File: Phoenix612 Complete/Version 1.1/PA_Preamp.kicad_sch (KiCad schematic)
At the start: 21 parts, among them J14 TP, J15 TP, U8 LT1253, U9 QPR_Filter

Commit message: Update 9Mar23
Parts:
- removed J14, J15: TP, Connector_PinHeader_1.00mm:PinHeader_1x01_P1.00mm_Vertical, symbol Connector_Generic:Conn_01x01
- added J14: TP11, Connector_PinSocket_2.54mm:PinSocket_1x02_P2.54mm_Vertical, symbol Connector_Generic:Conn_01x02
- added J15: TP12, Connector_PinSocket_2.54mm:PinSocket_1x02_P2.54mm_Vertical, symbol Connector_Generic:Conn_01x02
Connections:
- net GND: now also J14.2 (Pin_2), J15.2 (Pin_2)
- net PA_DRIVER_IN: now also J15.1 (Pin_1)
- net at C61.1, U9.7 (OUT), U9.8 (OUT): now also J14.1 (Pin_1)
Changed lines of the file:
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@@
   (junction (at 103.505 92.71) (diameter 0) (color 0 0 0 0)
   )
+  (junction (at 189.865 96.52) (diameter 0) (color 0 0 0 0)
+  )
   (junction (at 154.94 110.49) (diameter 0) (color 0 0 0 0)
   )
@@
   )
   (junction (at 139.065 92.71) (diameter 0) (color 0 0 0 0)
-  )
-  (junction (at 196.215 96.52) (diameter 0) (color 0 0 0 0)
   )
   (no_connect (at 180.34 111.125))
@@
     (stroke (width 0) (type default) (color 0 0 0 0))
   )
+  (wire (pts (xy 189.865 96.52) (xy 203.2 96.52))
+    (stroke (width 0) (type default) (color 0 0 0 0))
+  )
   (wire (pts (xy 161.29 83.82) (xy 152.4 83.82))
     (stroke (width 0) (type default) (color 0 0 0 0))
   )
+  (wire (pts (xy 139.065 90.805) (xy 139.065 92.71))
+    (stroke (width 0) (type default) (color 0 0 0 0))
+  )
   (wire (pts (xy 217.17 63.5) (xy 217.17 74.93))
     (stroke (width 0) (type default) (color 0 0 0 0))
@@
     (stroke (width 0) (type default) (color 0 0 0 0))
   )
+  (wire (pts (xy 130.81 90.805) (xy 139.065 90.805))
+    (stroke (width 0) (type default) (color 0 0 0 0))
+  )
   (wire (pts (xy 169.545 60.96) (xy 169.545 63.5))
     (stroke (width 0) (type default) (color 0 0 0 0))
@@
     (stroke (width 0) (type default) (color 0 0 0 0))
   )
+  (wire (pts (xy 189.865 83.185) (xy 189.865 96.52))
+    (stroke (width 0) (type default) (color 0 0 0 0))
+  )
   (wire (pts (xy 111.125 97.79) (xy 111.125 100.33))
     (stroke (width 0) (type default) (color 0 0 0 0))
@@
     (stroke (width 0) (type default) (color 0 0 0 0))
   )
+  (wire (pts (xy 130.81 80.645) (xy 130.81 90.805))
+    (stroke (width 0) (type default) (color 0 0 0 0))
+  )
   (wire (pts (xy 139.065 92.71) (xy 142.24 92.71))
     (stroke (width 0) (type default) (color 0 0 0 0))
@@
     (stroke (width 0) (type default) (color 0 0 0 0))
   )
-  (wire (pts (xy 196.215 96.52) (xy 203.2 96.52))
-    (stroke (width 0) (type default) (color 0 0 0 0))
-  )
   (wire (pts (xy 229.87 45.72) (xy 229.87 55.88))
     (stroke (width 0) (type default) (color 0 0 0 0))
@@
     (stroke (width 0) (type default) (color 0 0 0 0))
   )
-  (wire (pts (xy 186.69 96.52) (xy 196.215 96.52))
+  (wire (pts (xy 186.69 96.52) (xy 189.865 96.52))
     (stroke (width 0) (type default) (color 0 0 0 0))
   )
@@
   )
   (wire (pts (xy 131.445 105.41) (xy 131.445 100.33))
+    (stroke (width 0) (type default) (color 0 0 0 0))
+  )
+  (wire (pts (xy 133.35 80.645) (xy 133.35 83.185))
     (stroke (width 0) (type default) (color 0 0 0 0))
   )
@@
     (pin "1")
   )
+  (symbol (lib_id "power:GND") (at 192.405 83.185 0) (unit 1)
+    (in_bom yes) (on_board yes)
+    (property "Reference" "#PWR0107" (id 0) (at 192.405 89.535 0)
+      (effects (font (size 1.27 1.27)) hide)
+    )
+    (property "Value" "GND" (id 1) (at 192.405 86.995 0))
+    (property "Footprint" "" (id 2) (at 192.405 83.185 0)
+      (effects (font (size 1.27 1.27)) hide)
+    )
+    (property "Datasheet" "" (id 3) (at 192.405 83.185 0)
+      (effects (font (size 1.27 1.27)) hide)
+    )
+    (pin "1")
+  )
   (symbol (lib_id "Custom_RF:LT1253") (at 207.645 59.69 0) (unit 3)
     (in_bom yes) (on_board yes) (fields_autoplaced)
@@
     (pin "2")
   )
-  (symbol (lib_id "Connector_Generic:Conn_01x01") (at 139.065 87.63 90) (unit 1)
-    (in_bom yes) (on_board yes) (fields_autoplaced)
-    (property "Reference" "J14" (id 0) (at 141.605 86.3599 90)
-      (effects (font (size 1.27 1.27)) (justify right))
-    )
-    (property "Value" "TP" (id 1) (at 141.605 88.8999 90)
-      (effects (font (size 1.27 1.27)) (justify right))
-    )
-    (property "Footprint" "Connector_PinHeader_1.00mm:PinHeader_1x01_P1.00mm_Vertical" (id 2) (at 139.065 87.63 0)
-      (effects (font (size 1.27 1.27)) hide)
-    )
-    (property "Datasheet" "~" (id 3) (at 139.065 87.63 0)
-      (effects (font (size 1.27 1.27)) hide)
-    )
-    (pin "1")
-  )
   (symbol (lib_id "Device:C") (at 169.545 67.31 0) (unit 1)
     (in_bom yes) (on_board yes) (fields_autoplaced)
@@
     )
     (property "Datasheet" "" (id 3) (at 152.4 73.66 0)
-      (effects (font (size 1.27 1.27)) hide)
-    )
-    (pin "1")
-  )
-  (symbol (lib_id "Connector_Generic:Conn_01x01") (at 196.215 91.44 90) (unit 1)
-    (in_bom yes) (on_board yes) (fields_autoplaced)
-    (property "Reference" "J15" (id 0) (at 198.755 90.1699 90)
-      (effects (font (size 1.27 1.27)) (justify right))
-    )
-    (property "Value" "TP" (id 1) (at 198.755 92.7099 90)
-      (effects (font (size 1.27 1.27)) (justify right))
-    )
-    (property "Footprint" "Connector_PinHeader_1.00mm:PinHeader_1x01_P1.00mm_Vertical" (id 2) (at 196.215 91.44 0)
-      (effects (font (size 1.27 1.27)) hide)
-    )
-    (property "Datasheet" "~" (id 3) (at 196.215 91.44 0)
       (effects (font (size 1.27 1.27)) hide)
     )
@@
     )
     (property "Datasheet" "~" (id 3) (at 161.29 71.12 0)
+      (effects (font (size 1.27 1.27)) hide)
+    )
+    (pin "1")
+    (pin "2")
+  )
+  (symbol (lib_id "Connector_Generic:Conn_01x02") (at 189.865 78.105 90) (unit 1)
+    (in_bom yes) (on_board yes) (fields_autoplaced)
+    (property "Reference" "J15" (id 0) (at 195.58 76.8349 90)
+      (effects (font (size 1.27 1.27)) (justify right))
+    )
+    (property "Value" "TP12" (id 1) (at 195.58 79.3749 90)
+      (effects (font (size 1.27 1.27)) (justify right))
+    )
+    (property "Footprint" "Connector_PinSocket_2.54mm:PinSocket_1x02_P2.54mm_Vertical" (id 2) (at 189.865 78.105 0)
+      (effects (font (size 1.27 1.27)) hide)
+    )
+    (property "Datasheet" "~" (id 3) (at 189.865 78.105 0)
       (effects (font (size 1.27 1.27)) hide)
     )
@@
     (pin "1")
   )
+  (symbol (lib_id "power:GND") (at 133.35 83.185 0) (unit 1)
+    (in_bom yes) (on_board yes)
+    (property "Reference" "#PWR0106" (id 0) (at 133.35 89.535 0)
+      (effects (font (size 1.27 1.27)) hide)
+    )
+    (property "Value" "GND" (id 1) (at 133.35 86.995 0))
+    (property "Footprint" "" (id 2) (at 133.35 83.185 0)
+      (effects (font (size 1.27 1.27)) hide)
+    )
+    (property "Datasheet" "" (id 3) (at 133.35 83.185 0)
+      (effects (font (size 1.27 1.27)) hide)
+    )
+    (pin "1")
+  )
+  (symbol (lib_id "Connector_Generic:Conn_01x02") (at 130.81 75.565 90) (unit 1)
+    (in_bom yes) (on_board yes)
+    (property "Reference" "J14" (id 0) (at 126.365 72.39 90)
+      (effects (font (size 1.27 1.27)) (justify right))
+    )
+    (property "Value" "TP11" (id 1) (at 123.825 74.93 90)
+      (effects (font (size 1.27 1.27)) (justify right))
+    )
+    (property "Footprint" "Connector_PinSocket_2.54mm:PinSocket_1x02_P2.54mm_Vertical" (id 2) (at 130.81 75.565 0)
+      (effects (font (size 1.27 1.27)) hide)
+    )
+    (property "Datasheet" "~" (id 3) (at 130.81 75.565 0)
+      (effects (font (size 1.27 1.27)) hide)
+    )
+    (pin "1")
+    (pin "2")
+  )
 )

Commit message: Update 17Mar23
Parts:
- renumbered C55 to C56, C56 to C57, C57 to C58, C58 to C59, C59 to C60, C60 to C61, C61 to C62, C62 to C63, J14 to J18, J15 to J19, R41 to R40, R42 to R41, R43 to R42, R44 to R43, R45 to R44, R46 to R45
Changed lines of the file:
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@@
   (symbol (lib_id "Device:R_US") (at 163.83 110.49 90) (unit 1)
     (in_bom yes) (on_board yes) (fields_autoplaced)
-    (property "Reference" "R45" (id 0) (at 163.83 104.14 90))
+    (property "Reference" "R44" (id 0) (at 163.83 104.14 90))
     (property "Value" "620" (id 1) (at 163.83 106.68 90))
     (property "Footprint" "Resistor_SMD:R_1206_3216Metric" (id 2) (at 164.084 109.474 90)
@@
   (symbol (lib_id "power:GND") (at 154.94 142.24 0) (unit 1)
     (in_bom yes) (on_board yes) (fields_autoplaced)
-    (property "Reference" "#PWR058" (id 0) (at 154.94 148.59 0)
+    (property "Reference" "#PWR078" (id 0) (at 154.94 148.59 0)
       (effects (font (size 1.27 1.27)) hide)
     )
@@
   (symbol (lib_id "Device:R_US") (at 154.94 128.27 0) (unit 1)
     (in_bom yes) (on_board yes) (fields_autoplaced)
-    (property "Reference" "R46" (id 0) (at 157.48 126.9999 0)
+    (property "Reference" "R45" (id 0) (at 157.48 126.9999 0)
       (effects (font (size 1.27 1.27)) (justify left))
     )
@@
   (symbol (lib_id "power:GND") (at 83.185 95.885 0) (unit 1)
     (in_bom yes) (on_board yes) (fields_autoplaced)
-    (property "Reference" "#PWR056" (id 0) (at 83.185 102.235 0)
+    (property "Reference" "#PWR076" (id 0) (at 83.185 102.235 0)
       (effects (font (size 1.27 1.27)) hide)
     )
@@
   (symbol (lib_id "power:GND") (at 192.405 83.185 0) (unit 1)
     (in_bom yes) (on_board yes)
-    (property "Reference" "#PWR0107" (id 0) (at 192.405 89.535 0)
+    (property "Reference" "#PWR075" (id 0) (at 192.405 89.535 0)
       (effects (font (size 1.27 1.27)) hide)
     )
@@
   (symbol (lib_id "power:GND") (at 217.17 77.47 0) (unit 1)
     (in_bom yes) (on_board yes) (fields_autoplaced)
-    (property "Reference" "#PWR055" (id 0) (at 217.17 83.82 0)
+    (property "Reference" "#PWR073" (id 0) (at 217.17 83.82 0)
       (effects (font (size 1.27 1.27)) hide)
     )
@@
   (symbol (lib_id "Device:C") (at 140.97 67.945 0) (unit 1)
     (in_bom yes) (on_board yes) (fields_autoplaced)
-    (property "Reference" "C59" (id 0) (at 144.78 66.6749 0)
+    (property "Reference" "C60" (id 0) (at 144.78 66.6749 0)
       (effects (font (size 1.27 1.27)) (justify left))
     )
@@
   (symbol (lib_id "Device:R_US") (at 152.4 67.31 0) (unit 1)
     (in_bom yes) (on_board yes) (fields_autoplaced)
-    (property "Reference" "R42" (id 0) (at 154.94 66.0399 0)
+    (property "Reference" "R41" (id 0) (at 154.94 66.0399 0)
       (effects (font (size 1.27 1.27)) (justify left))
     )
@@
   (symbol (lib_id "power:GND") (at 140.97 73.66 0) (unit 1)
     (in_bom yes) (on_board yes) (fields_autoplaced)
-    (property "Reference" "#PWR053" (id 0) (at 140.97 80.01 0)
+    (property "Reference" "#PWR071" (id 0) (at 140.97 80.01 0)
       (effects (font (size 1.27 1.27)) hide)
     )
@@
   (symbol (lib_id "power:GND") (at 169.545 73.025 0) (unit 1)
     (in_bom yes) (on_board yes) (fields_autoplaced)
-    (property "Reference" "#PWR052" (id 0) (at 169.545 79.375 0)
+    (property "Reference" "#PWR070" (id 0) (at 169.545 79.375 0)
       (effects (font (size 1.27 1.27)) hide)
     )
@@
   (symbol (lib_id "Device:C") (at 240.665 59.69 0) (unit 1)
     (in_bom yes) (on_board yes) (fields_autoplaced)
-    (property "Reference" "C57" (id 0) (at 244.475 58.4199 0)
+    (property "Reference" "C58" (id 0) (at 244.475 58.4199 0)
       (effects (font (size 1.27 1.27)) (justify left))
     )
@@
   (symbol (lib_id "Device:R_US") (at 152.4 55.88 0) (unit 1)
     (in_bom yes) (on_board yes) (fields_autoplaced)
-    (property "Reference" "R41" (id 0) (at 154.94 54.6099 0)
+    (property "Reference" "R40" (id 0) (at 154.94 54.6099 0)
       (effects (font (size 1.27 1.27)) (justify left))
     )
@@
   (symbol (lib_id "Device:C") (at 169.545 67.31 0) (unit 1)
     (in_bom yes) (on_board yes) (fields_autoplaced)
-    (property "Reference" "C58" (id 0) (at 172.72 66.0399 0)
+    (property "Reference" "C59" (id 0) (at 172.72 66.0399 0)
       (effects (font (size 1.27 1.27)) (justify left))
     )
@@
   (symbol (lib_id "Device:C") (at 217.17 59.69 0) (unit 1)
     (in_bom yes) (on_board yes) (fields_autoplaced)
-    (property "Reference" "C55" (id 0) (at 220.98 58.4199 0)
+    (property "Reference" "C56" (id 0) (at 220.98 58.4199 0)
       (effects (font (size 1.27 1.27)) (justify left))
     )
@@
   (symbol (lib_id "Device:C") (at 154.94 137.16 0) (unit 1)
     (in_bom yes) (on_board yes) (fields_autoplaced)
-    (property "Reference" "C62" (id 0) (at 158.75 135.8899 0)
+    (property "Reference" "C63" (id 0) (at 158.75 135.8899 0)
       (effects (font (size 1.27 1.27)) (justify left))
     )
@@
   (symbol (lib_id "power:GND") (at 152.4 73.66 0) (unit 1)
     (in_bom yes) (on_board yes) (fields_autoplaced)
-    (property "Reference" "#PWR054" (id 0) (at 152.4 80.01 0)
+    (property "Reference" "#PWR072" (id 0) (at 152.4 80.01 0)
       (effects (font (size 1.27 1.27)) hide)
     )
@@
   (symbol (lib_id "Device:C") (at 75.565 83.82 90) (unit 1)
     (in_bom yes) (on_board yes) (fields_autoplaced)
-    (property "Reference" "C60" (id 0) (at 75.565 76.2 90))
+    (property "Reference" "C61" (id 0) (at 75.565 76.2 90))
     (property "Value" "10n" (id 1) (at 75.565 78.74 90))
     (property "Footprint" "Capacitor_SMD:C_1206_3216Metric" (id 2) (at 79.375 82.8548 0)
@@
   (symbol (lib_id "Device:R_US") (at 161.29 71.12 180) (unit 1)
     (in_bom yes) (on_board yes)
-    (property "Reference" "R43" (id 0) (at 163.83 69.85 0)
+    (property "Reference" "R42" (id 0) (at 163.83 69.85 0)
       (effects (font (size 1.27 1.27)) (justify right))
     )
@@
   (symbol (lib_id "Connector_Generic:Conn_01x02") (at 189.865 78.105 90) (unit 1)
     (in_bom yes) (on_board yes) (fields_autoplaced)
-    (property "Reference" "J15" (id 0) (at 195.58 76.8349 90)
+    (property "Reference" "J19" (id 0) (at 195.58 76.8349 90)
       (effects (font (size 1.27 1.27)) (justify right))
     )
@@
   (symbol (lib_id "Device:R_US") (at 182.88 96.52 90) (unit 1)
     (in_bom yes) (on_board yes) (fields_autoplaced)
-    (property "Reference" "R44" (id 0) (at 182.88 90.17 90))
+    (property "Reference" "R43" (id 0) (at 182.88 90.17 90))
     (property "Value" "50R" (id 1) (at 182.88 92.71 90))
     (property "Footprint" "Resistor_SMD:R_1206_3216Metric" (id 2) (at 183.134 95.504 90)
@@
   (symbol (lib_id "power:PWR_FLAG") (at 205.74 45.72 0) (unit 1)
     (in_bom yes) (on_board yes)
-    (property "Reference" "#FLG011" (id 0) (at 205.74 43.815 0)
+    (property "Reference" "#FLG012" (id 0) (at 205.74 43.815 0)
       (effects (font (size 1.27 1.27)) hide)
     )
@@
   (symbol (lib_id "Device:C") (at 146.05 92.71 90) (unit 1)
     (in_bom yes) (on_board yes) (fields_autoplaced)
-    (property "Reference" "C61" (id 0) (at 146.05 85.09 90))
+    (property "Reference" "C62" (id 0) (at 146.05 85.09 90))
     (property "Value" "100n" (id 1) (at 146.05 87.63 90))
     (property "Footprint" "Capacitor_SMD:C_1206_3216Metric" (id 2) (at 149.86 91.7448 0)
@@
   (symbol (lib_id "Device:C_Polarized") (at 229.87 59.69 0) (unit 1)
     (in_bom yes) (on_board yes) (fields_autoplaced)
-    (property "Reference" "C56" (id 0) (at 233.68 57.5309 0)
+    (property "Reference" "C57" (id 0) (at 233.68 57.5309 0)
       (effects (font (size 1.27 1.27)) (justify left))
     )
@@
   (symbol (lib_id "power:GND") (at 121.285 107.95 0) (unit 1)
     (in_bom yes) (on_board yes) (fields_autoplaced)
-    (property "Reference" "#PWR057" (id 0) (at 121.285 114.3 0)
+    (property "Reference" "#PWR077" (id 0) (at 121.285 114.3 0)
       (effects (font (size 1.27 1.27)) hide)
     )
@@
   (symbol (lib_id "power:GND") (at 133.35 83.185 0) (unit 1)
     (in_bom yes) (on_board yes)
-    (property "Reference" "#PWR0106" (id 0) (at 133.35 89.535 0)
+    (property "Reference" "#PWR074" (id 0) (at 133.35 89.535 0)
       (effects (font (size 1.27 1.27)) hide)
     )
@@
   (symbol (lib_id "Connector_Generic:Conn_01x02") (at 130.81 75.565 90) (unit 1)
     (in_bom yes) (on_board yes)
-    (property "Reference" "J14" (id 0) (at 126.365 72.39 90)
-      (effects (font (size 1.27 1.27)) (justify right))
-    )
+    (property "Reference" "J18" (id 0) (at 126.365 72.39 90)
+      (effects (font (size 1.27 1.27)) (justify right))
+    )

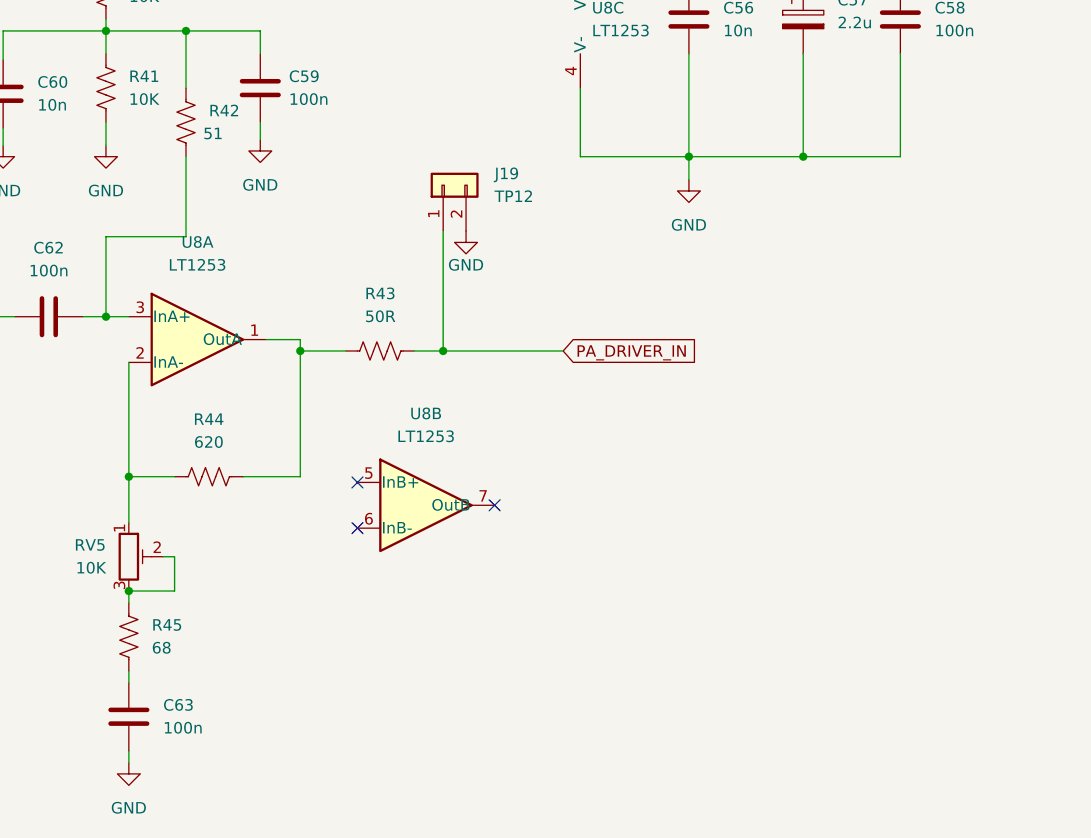
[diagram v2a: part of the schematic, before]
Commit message: Update LT1253 Tx
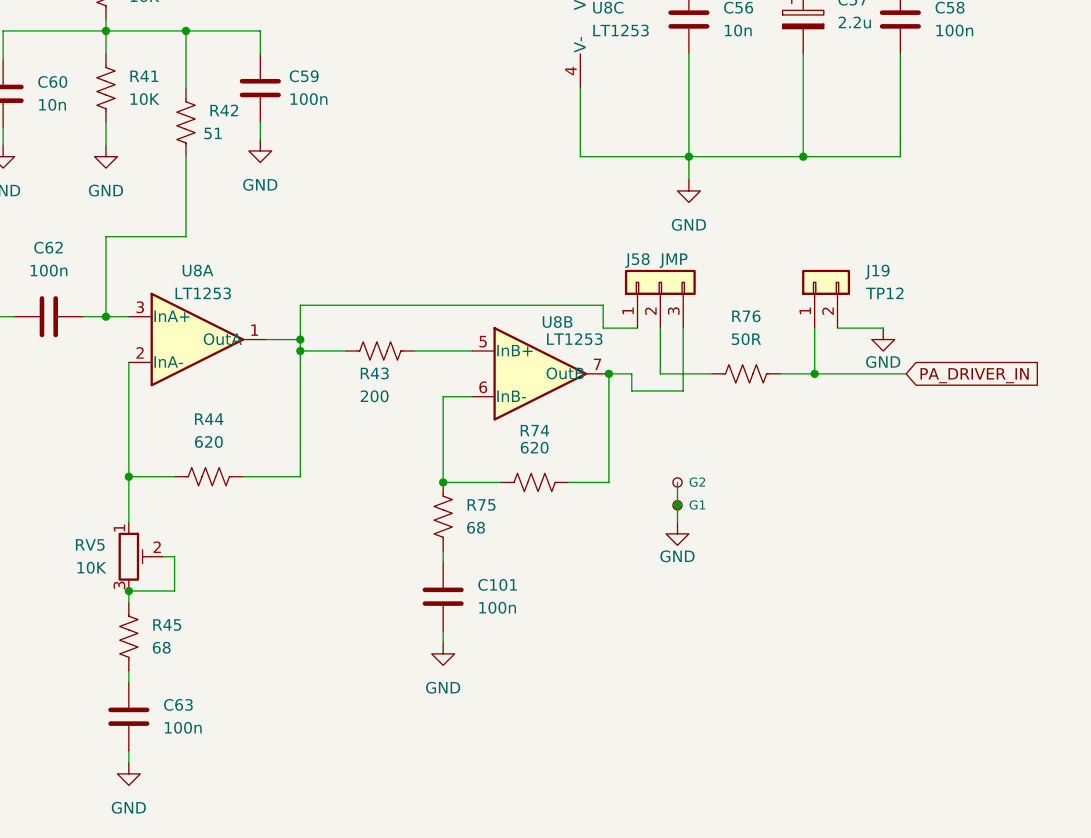
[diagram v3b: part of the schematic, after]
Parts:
- added C101: 100n, Capacitor_SMD:C_1206_3216Metric, symbol Device:C
- added G1, G2: GND, TestPoint:TestPoint_Pad_D1.0mm, symbol Connector:TestPoint_Small
- added J58: JMP, Connector_PinSocket_2.54mm:PinSocket_1x03_P2.54mm_Vertical, symbol Connector_Generic:Conn_01x03
- added R74: 620, Resistor_SMD:R_1206_3216Metric, symbol Device:R_US
- added R75: 68, Resistor_SMD:R_1206_3216Metric, symbol Device:R_US
- added R76: 50R, Resistor_SMD:R_1206_3216Metric, symbol Device:R_US
- R43: value 50R -> 200
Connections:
- net GND: now also C101.2, G1.1, G2.1
- net PA_DRIVER_IN: now also R76.2; no longer R43.2
- net at R43.1, R44.2, U8.1 (OutA): now also J58.1 (Pin_1)
- net at U8.5 (InB+): now also R43.2
- net at U8.6 (InB-): now also R74.1, R75.1
- net at U8.7 (OutB): now also J58.3 (Pin_3), R74.2
- new net: C101.1, R75.2
- new net: J58.2 (Pin_2), R76.1
- no-connect marks 3 -> 0
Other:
- moved on the sheet: J19, U8B
